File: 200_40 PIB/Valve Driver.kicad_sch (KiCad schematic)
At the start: 40 parts, among them J4 53398-0671, Q10 IRF7832, U1 LT3065EDDPBF, U2 MIC4424YM, U3 MIC4424YM, U6 LM1117MP-3.3, U8 74LVC1GU04DRL, U9 74LVC2G126DCU

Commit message: correct symbol link for lt3065
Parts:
- removed U1: LT3065EDDPBF, 0_PAY_Footprint_Library:DFN-10_DD, symbol LT3065EDDPBF:LT3065EDDPBF
- added U1: LT3065EDDPBF, 0_PAY_Footprint_Library:DFN-10_DD, symbol 0_PAY_Symbol_Library:LT3065EDDPBF
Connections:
- net +12V: now also U1.10 (OUT), U1.9 (OUT)
- net BAT_HOT: now also U1.1 (IN), U1.2 (IN), U1.3 (*SHDN)
- net GND: now also U1.11 (GND), U1.7 (GND/ADJ)
- net at C22.2, R17.1, R18.2: now also U1.8 (ADJ/SENSE)
- net at C10.1, R2.2: now also U1.5 (IMAX)
- net at R1.2: now also U1.4 (PWRGD)
- net at C11.1: now also U1.6 (REF/BYP)
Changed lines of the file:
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@@
 	)
 	(junction
+		(at 35.56 22.86)
+		(diameter 0)
+		(color 0 0 0 0)
+	)
+	(junction
 		(at 125.73 83.82)
 		(diameter 0)
@@
 	)
 	(junction
-		(at 35.56 22.86)
-		(diameter 0)
-		(color 0 0 0 0)
-	)
-	(junction
-		(at 35.56 30.48)
+		(at 152.4 55.88)
 		(diameter 0)
 		(color 0 0 0 0)
 	)
 	(junction
-		(at 152.4 55.88)
+		(at 27.94 22.86)
 		(diameter 0)
 		(color 0 0 0 0)
 	)
 	(junction
-		(at 27.94 22.86)
+		(at 35.56 30.48)
 		(diameter 0)
 		(color 0 0 0 0)
@@
 	(wire
 		(pts
+			(xy 58.42 27.94) (xy 68.58 27.94)
+		)
+		(stroke
+			(width 0)
+			(type default)
+		)
+	)
+	(wire
+		(pts
 			(xy 138.43 50.8) (xy 144.78 50.8)
 		)
@@
 	(wire
 		(pts
-			(xy 58.42 25.4) (xy 72.39 25.4)
+			(xy 35.56 22.86) (xy 35.56 25.4)
 		)
 		(stroke
@@
 	(wire
 		(pts
-			(xy 35.56 22.86) (xy 35.56 25.4)
+			(xy 58.42 25.4) (xy 72.39 25.4)
 		)
 		(stroke
@@
 	(wire
 		(pts
-			(xy 58.42 27.94) (xy 68.58 27.94)
-		)
-		(stroke
-			(width 0)
-			(type default)
-		)
-	)
-	(wire
-		(pts
 			(xy 190.5 109.22) (xy 204.47 109.22)
 		)
@@
 	)
 	(symbol
+		(lib_id "0_PAY_Symbol_Library:LT3065EDDPBF")
+		(at 30.48 22.86 0)
+		(unit 1)
+		(body_style 1)
+		(exclude_from_sim no)
+		(in_bom yes)
+		(on_board yes)
+		(in_pos_files yes)
+		(dnp no)
+		(fields_autoplaced yes)
+		(property "Reference" "U1"
+			(at 46.99 15.24 0)
+			(show_name no)
+			(do_not_autoplace no)
+			(effects
+				(font
+					(size 1.27 1.27)
+				)
+			)
+		)
+		(property "Value" "LT3065EDDPBF"
+			(at 46.99 17.78 0)
+			(show_name no)
+			(do_not_autoplace no)
+			(effects
+				(font
+					(size 1.27 1.27)
+				)
+			)
+		)
+		(property "Footprint" "0_PAY_Footprint_Library:DFN-10_DD"
+			(at 30.48 22.86 0)
+			(hide yes)
+			(show_name no)
+			(do_not_autoplace no)
+			(effects
+				(font
+					(size 1.27 1.27)
+				)
+				(justify bottom)
+			)
+		)
+		(property "Datasheet" ""
+			(at 30.48 22.86 0)
+			(hide yes)
+			(show_name no)
+			(do_not_autoplace no)
+			(effects
+				(font
+					(size 1.27 1.27)
+				)
+			)
+		)
+		(property "Description" "Linear Voltage Regulator IC Positive Adjustable 1 Output  500mA 10-DFN (3x3)"
+			(at 29.21 19.05 0)
+			(hide yes)
+			(show_name no)
+			(do_not_autoplace no)
+			(effects
+				(font
+					(size 1.27 1.27)
+				)
+				(justify bottom)
+			)
+		)
+		(property "MF" "Analog Devices"
+			(at 30.48 22.86 0)
+			(hide yes)
+			(show_name no)
+			(do_not_autoplace no)
+			(effects
+				(font
+					(size 1.27 1.27)
+				)
+				(justify bottom)
+			)
+		)
+		(property "VENDOR" "Linear Technology"
+			(at 30.48 22.86 0)
+			(hide yes)
+			(show_name no)
+			(do_not_autoplace no)
+			(effects
+				(font
+					(size 1.27 1.27)
+				)
+				(justify bottom)
+			)
+		)
+		(property "Package" "DFN-10 Linear Technology"
+			(at 30.48 22.86 0)
+			(hide yes)
+			(show_name no)
+			(do_not_autoplace no)
+			(effects
+				(font
+					(size 1.27 1.27)
+				)
+				(justify bottom)
+			)
+		)
+		(property "Price" "None"
+			(at 30.48 22.86 0)
+			(hide yes)
+			(show_name no)
+			(do_not_autoplace no)
+			(effects
+				(font
+					(size 1.27 1.27)
+				)
+				(justify bottom)
+			)
+		)
+		(property "MP" "LT3065EDD#PBF"
+			(at 30.48 22.86 0)
+			(hide yes)
+			(show_name no)
+			(do_not_autoplace no)
+			(effects
+				(font
+					(size 1.27 1.27)
+				)
+				(justify bottom)
+			)
+		)
+		(pin "7"
+		)
+		(pin "5"
+		)
+		(pin "4"
+		)
+		(pin "8"
+		)
+		(pin "1"
+		)
+		(pin "10"
+		)
+		(pin "11"
+		)
+		(pin "3"
+		)
+		(pin "9"
+		)
+		(pin "2"
+		)
+		(pin "6"
+		)
+		(instances
+			(project "PIB"
+				(path "/2bb2e4a1-de70-477a-a246-143db0a21e08/a3e2437a-f450-49da-ac0f-e1add7c59a42"
+					(reference "U1")
+					(unit 1)
+				)
+			)
+		)
+	)
+	(symbol
 		(lib_id "Device:R")
 		(at 148.59 50.8 90)
@@
 					(unit 1)
 				)
-			)
-		)
-	)
-	(symbol
-		(lib_id "LT3065EDDPBF:LT3065EDDPBF")
-		(at 30.48 22.86 0)
-		(unit 1)
-		(body_style 1)
-		(exclude_from_sim no)
-		(in_bom yes)
-		(on_board yes)
-		(in_pos_files yes)
-		(dnp no)
-		(fields_autoplaced yes)
-		(property "Reference" "U1"
-			(at 46.99 15.24 0)
-			(show_name no)
-			(do_not_autoplace no)
-			(effects
-				(font
-					(size 1.27 1.27)
-				)
-			)
-		)
-		(property "Value" "LT3065EDDPBF"
-			(at 46.99 17.78 0)
-			(show_name no)
-			(do_not_autoplace no)
-			(effects
-				(font
-					(size 1.27 1.27)
-				)
-			)
-		)
-		(property "Footprint" "0_PAY_Footprint_Library:DFN-10_DD"
-			(at 30.48 22.86 0)
-			(hide yes)
-			(show_name no)
-			(do_not_autoplace no)
-			(effects
-				(font
-					(size 1.27 1.27)
-				)
-				(justify bottom)
-			)
-		)
-		(property "Datasheet" ""
-			(at 30.48 22.86 0)
-			(hide yes)
-			(show_name no)
-			(do_not_autoplace no)
-			(effects
-				(font
-					(size 1.27 1.27)
-				)
-			)
-		)
-		(property "Description" "Linear Voltage Regulator IC Positive Adjustable 1 Output  500mA 10-DFN (3x3)"
-			(at 29.21 19.05 0)
-			(hide yes)
-			(show_name no)
-			(do_not_autoplace no)
-			(effects
-				(font
-					(size 1.27 1.27)
-				)
-				(justify bottom)
-			)
-		)
-		(property "MF" "Analog Devices"
-			(at 30.48 22.86 0)
-			(hide yes)
-			(show_name no)
-			(do_not_autoplace no)
-			(effects
-				(font
-					(size 1.27 1.27)
-				)
-				(justify bottom)
-			)
-		)
-		(property "VENDOR" "Linear Technology"
-			(at 30.48 22.86 0)
-			(hide yes)
-			(show_name no)
-			(do_not_autoplace no)
-			(effects
-				(font
-					(size 1.27 1.27)
-				)
-				(justify bottom)
-			)
-		)
-		(property "Package" "DFN-10 Linear Technology"
-			(at 30.48 22.86 0)
-			(hide yes)
-			(show_name no)
-			(do_not_autoplace no)
-			(effects
-				(font
-					(size 1.27 1.27)
-				)
-				(justify bottom)
-			)
-		)
-		(property "Price" "None"
-			(at 30.48 22.86 0)
-			(hide yes)
-			(show_name no)
-			(do_not_autoplace no)
-			(effects
-				(font
-					(size 1.27 1.27)
-				)
-				(justify bottom)
-			)
-		)
-		(property "MP" "LT3065EDD#PBF"
-			(at 30.48 22.86 0)
-			(hide yes)
-			(show_name no)
-			(do_not_autoplace no)
-			(effects
-				(font
-					(size 1.27 1.27)
-				)
-				(justify bottom)
-			)
-		)
-		(pin "10"
-		)
-		(pin "6"
-		)
-		(pin "2"
-		)
-		(pin "4"
-		)
-		(pin "1"
-		)
-		(pin "3"
-		)
-		(pin "8"
-		)
-		(pin "9"
-		)
-		(pin "11"
-		)
-		(pin "5"
-		)
-		(pin "7"
-		)
-		(instances
-			(project "PIB"
-				(path "/2bb2e4a1-de70-477a-a246-143db0a21e08/a3e2437a-f450-49da-ac0f-e1add7c59a42"
-					(reference "U1")
-					(unit 1)
-				)

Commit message: Fix MIC4424 library reference
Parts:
- removed U2, U3: MIC4424YM, Package_SO:SOIC-8_3.9x4.9mm_P1.27mm, symbol MIC4424YM:MIC4424YM
- added U2, U3: MIC4424YM, Package_SO:SOIC-8_3.9x4.9mm_P1.27mm, symbol 0_PAY_Symbol_Library:MIC4424YM
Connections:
- net +12V: now also U2.6 (VS), U3.6 (VS)
- net GND: now also U2.3 (GND), U3.3 (GND)
- net at R10.2, R42.1, U9.3: now also U3.2 (INA)
- net at R12.2, R40.1: now also U2.2 (INA)
- net at R11.2, R41.1, U9.6: now also U3.4 (INB)
- net at R38.2, R39.1: now also U2.4 (INB)
- net at J4.1 (Pin_1): now also U2.5 (OUTB)
- net at J4.2 (Pin_2): now also U2.7 (OUTA)
- net at J4.3 (Pin_3): now also U3.5 (OUTB)
- net at J4.4 (Pin_4): now also U3.7 (OUTA)

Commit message: fix GSE valve having no power path, fix arm/safe gate floating on reset, fix resistor OR on GSE NC valve, add NC valve flyback diode, change DPT MCLK source to a timer off of HSE, fix crystal load capacitances
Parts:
- added D11, D36, D37: NSVR1020MW2T1G, Diode_SMD:D_SOD-323, symbol Device:D_Schottky
- R47: value 1K -> 100R
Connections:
- net +12V: now also D11.1 (K), D36.1 (K), D37.1 (K); no longer C22.1, C6.1, R18.1, U1.10 (OUT), U1.9 (OUT)
- net 12V_GSE: now also D36.2 (A)
- net at J4.6 (Pin_6), Q10.5 (D), Q10.6 (D)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: now also D37.2 (A)
- new net: C22.1, C6.1, D11.2 (A), R18.1, U1.10 (OUT), U1.9 (OUT)

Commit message: clear out claude flagged items
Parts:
- removed R10, R11, R12, R38, R43, R5: 1K, Resistor_SMD:R_0402_1005Metric, symbol Device:R
- removed R44: 100K, Resistor_SMD:R_0402_1005Metric, symbol Device:R
- removed U8: 74LVC1GU04DRL, Package_TO_SOT_SMD:SOT-553, symbol 74xGxx:74LVC1GU04DRL
- removed U9: 74LVC2G126DCU, Package_SO:VSSOP-8_2.3x2mm_P0.5mm, symbol 74xGxx:74LVC2G126
- added C73, C74: 1uF, Capacitor_SMD:C_0402_1005Metric, symbol Device:C
- added C75: 100nF, Capacitor_SMD:C_0402_1005Metric, symbol Device:C
- added D41, D42: BAT54J, Diode_SMD:D_SOD-323F, symbol Diode:BAT54J
- added D47, D48, D50: BAT54C, Package_TO_SOT_SMD:SOT-23, symbol Diode:BAT54C
- added R107: 100K, Resistor_SMD:R_0402_1005Metric, symbol Device:R
- added R110: 100R, Resistor_SMD:R_0402_1005Metric, symbol Device:R
- added U18: 74LVC2G14, Package_TO_SOT_SMD:SOT-23-6, symbol 74xGxx:74LVC2G14
- added U9: 74LVC2G17, Package_TO_SOT_SMD:SOT-23-6, symbol 74xGxx:74LVC2G17
- R45: value 10K -> 100K; footprint Resistor_SMD:R_0603_1608Metric -> Resistor_SMD:R_0402_1005Metric
- R46: value 43K -> 1K; footprint Resistor_SMD:R_0603_1608Metric -> Resistor_SMD:R_0402_1005Metric
- R47: value 100R -> 100K
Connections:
- net 12V_GSE: no longer R46.2
- net 3.3V_EGSE: now also C75.1, U18.5 (VCC), U9.5 (VCC)
- net EGSE_OPEN: now also R46.2; no longer R47.1
- net GND: now also R45.2, R47.2, C75.2, D41.2 (A), D42.2 (A), R107.2, U18.2 (GND), U9.2 (GND); no longer R45.1
- net LHD1: now also D50.2
- net LHL1: now also R40.1, U2.2 (INA)
- net LHL2: now also R39.1, U2.4 (INB)
- net LHL3: now also D48.2
- net LHL4: now also D47.2
- net at R42.1, U3.2 (INA): now also D48.3
- net EGSE_OPEN_F: now reaches R46.1
- net EGSE_OPEN_F: now also R45.1, D50.1, U18.3; no longer R45.2
- net at Q10.4 (G), R6.1: now also R110.1; no longer R47.2
- net at R41.1, U3.4 (INB): now also D47.3
- new net: C74.2, D42.1 (K), R107.1, U9.1
- new net: D48.1, U9.6
- new net: D50.3, R110.2
- new net: C74.1, U18.1, U18.4
- new net: C73.1, U18.6
- new net: C73.2, D41.1 (K), R47.1, U9.3
- new net: D47.1, U9.4
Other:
- note added: "Doides to prevent backdrive"
- note removed: "Rough "UVLO" feature"
- note removed: "Tristate buffer ensures backdrive is not an issue"
- moved on the sheet: C1, C10, C11, C2, C22, C23, C24, C3, C31, C6, C68, C7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

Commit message: clod
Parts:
- R17: value 1.13K -> 1K
- R18: value 21.5K -> 20K
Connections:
- net BAT_HOT: no longer R1.1
- net 12V_PG: now reaches R1.2, U1.4 (PWRGD)
- new net +3.3V: R1.1
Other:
- note added: "12.6V Regulation to account for diode drop + droop"
- moved on the sheet: C1, C10, C11, C22, C6, D11, D36, R1, R17, R18, R2, U1

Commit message: lots of claude close outs
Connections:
- net BAT_HOT renamed VBAT_PROT
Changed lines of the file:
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@@
 		(in_pos_files yes)
 		(dnp no)
-		(fields_autoplaced yes)
 		(property "Reference" "#PWR013"
 			(at 24.13 36.83 0)
@@
 			)
 		)
-		(property "Value" "BAT_HOT"
-			(at 24.13 27.94 0)
+		(property "Value" "VBAT_PROT"
+			(at 24.13 28.956 0)
 			(show_name no)
 			(do_not_autoplace no)

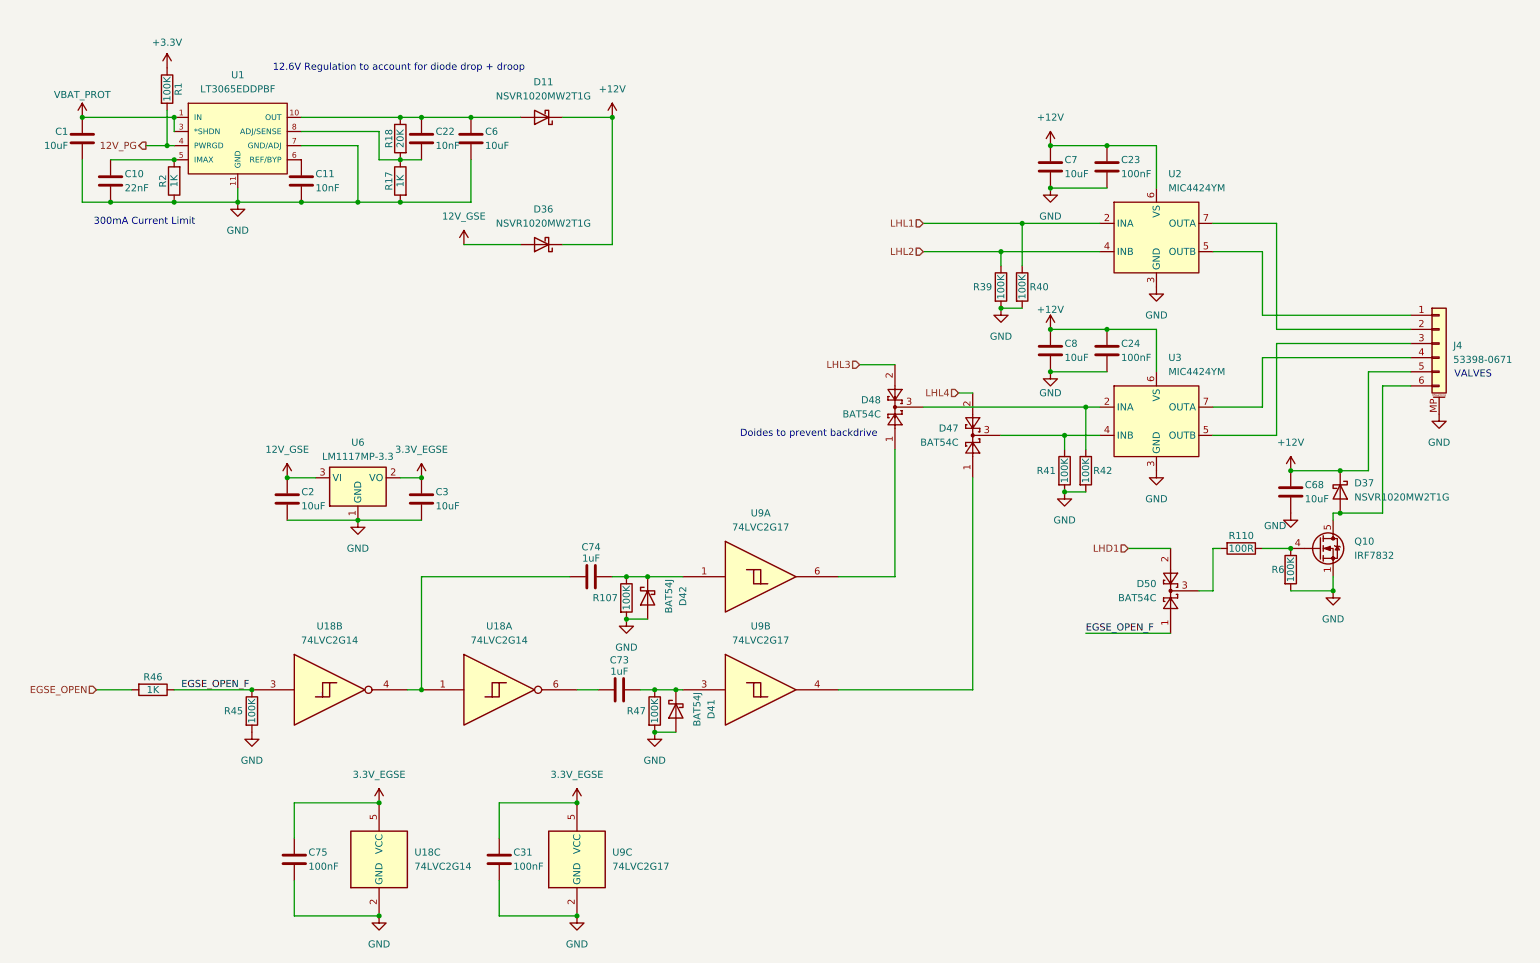
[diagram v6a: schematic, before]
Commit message: finish routing with all critical schematic fixes
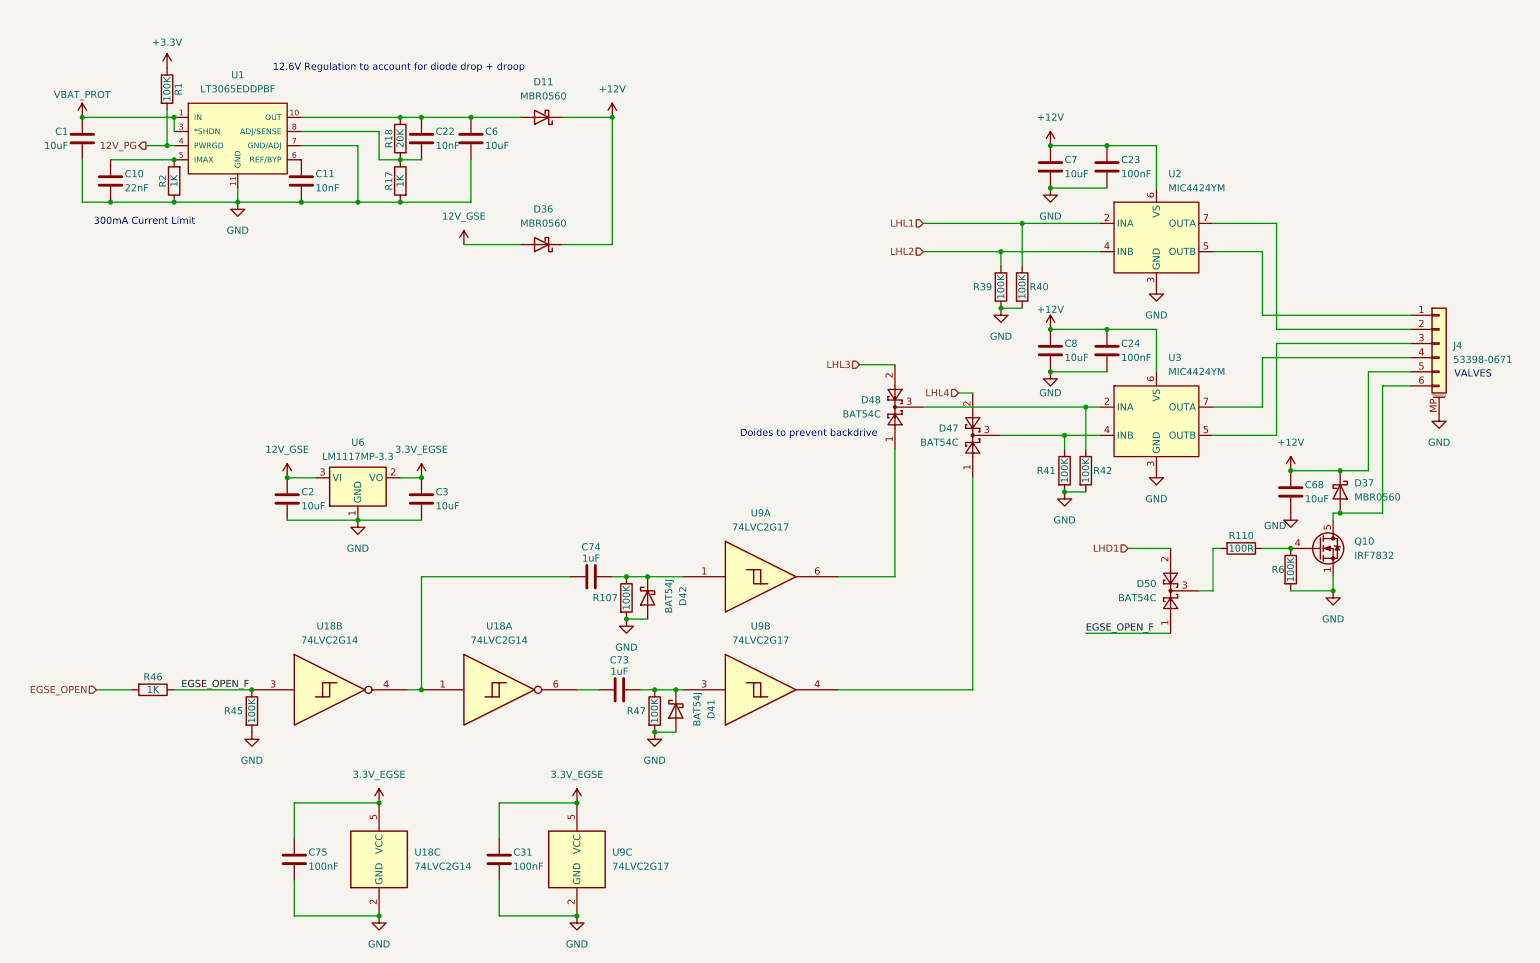
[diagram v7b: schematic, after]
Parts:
- removed D11, D36, D37: NSVR1020MW2T1G, Diode_SMD:D_SOD-323, symbol Device:D_Schottky
- added D11, D36, D37: MBR0560, Diode_SMD:D_SOD-123, symbol Diode:MBR0560
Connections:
- net +12V: now also D11.1 (K), D36.1 (K), D37.1 (K)
- net 12V_GSE: now also D36.2 (A)
- net at C22.1, C6.1, R18.1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: now also D11.2 (A)
- net at J4.6 (Pin_6), Q10.5 (D), Q10.6 (D)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: now also D37.2 (A)

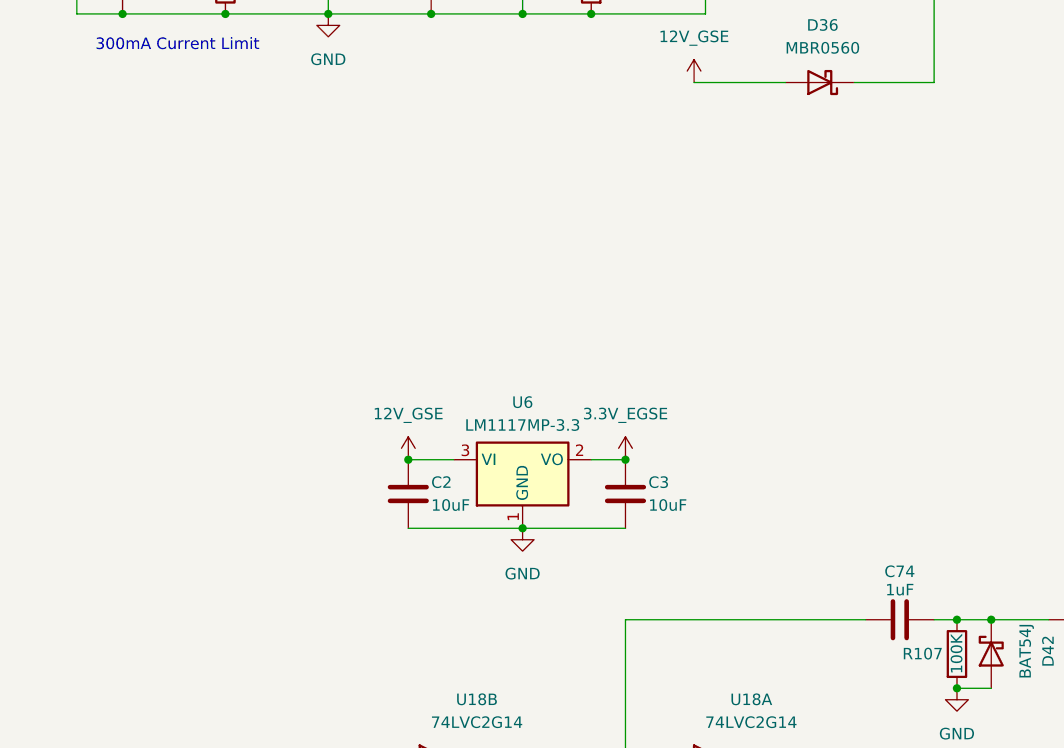
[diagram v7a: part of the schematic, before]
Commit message: add uvlo to gse valve drive
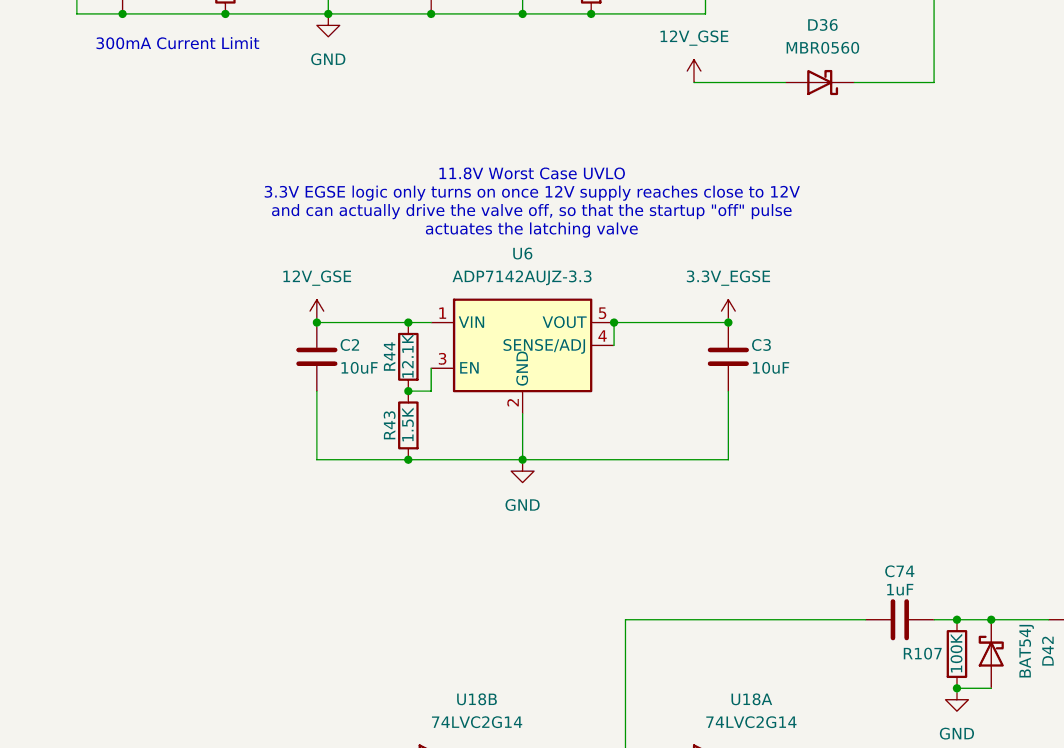
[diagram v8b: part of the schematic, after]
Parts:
- removed U6: LM1117MP-3.3, Package_TO_SOT_SMD:SOT-223-3_TabPin2, symbol Regulator_Linear:LM1117MP-3.3
- added R43: 1.5K, Resistor_SMD:R_0402_1005Metric, symbol Device:R
- added R44: 12.1K, Resistor_SMD:R_0402_1005Metric, symbol Device:R
- added U6: ADP7142AUJZ-3.3, Package_TO_SOT_SMD:TSOT-23-5, symbol Regulator_Linear:ADP7142AUJZ-3.3
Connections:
- net 12V_GSE: now also R44.1, U6.1 (VIN)
- net 3.3V_EGSE: now also U6.4 (SENSE/ADJ), U6.5 (VOUT)
- net GND: now also R43.2, U6.2 (GND)
- new net: R43.1, R44.2, U6.3 (EN)
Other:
- note added: "11.8V Worst Case UVLO 3.3V EGSE logic only turns on once 12V supply reaches close to 12V and can actually drive the valve off, so that the startup "off" pulse actuates the latching valve"
- moved on the sheet: C2, C3
